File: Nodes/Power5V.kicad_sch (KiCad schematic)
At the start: 15 parts, among them U4 LT3970EMS#TRPBF

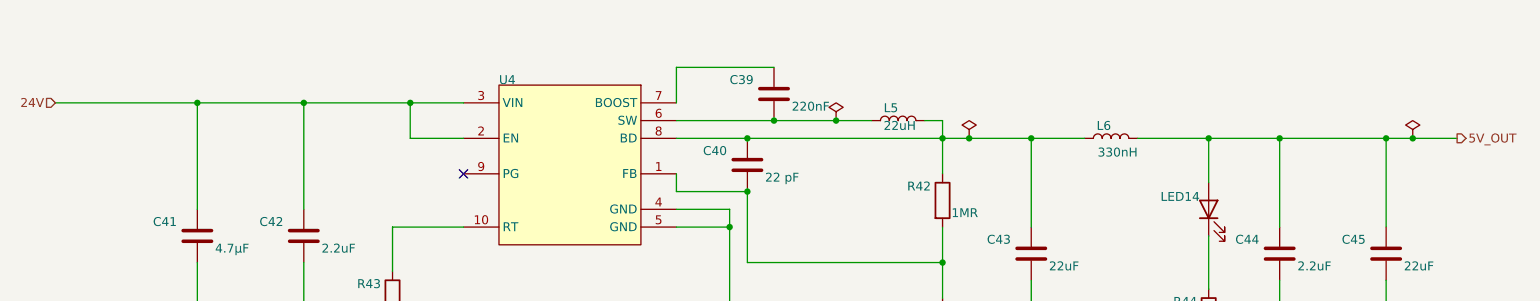
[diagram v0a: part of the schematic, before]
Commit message: Nodes v2.1.2 Improved
- Improved schematic design
- Added two 4.7 uF caps according to the datasheets of the microchips
- Other small changes
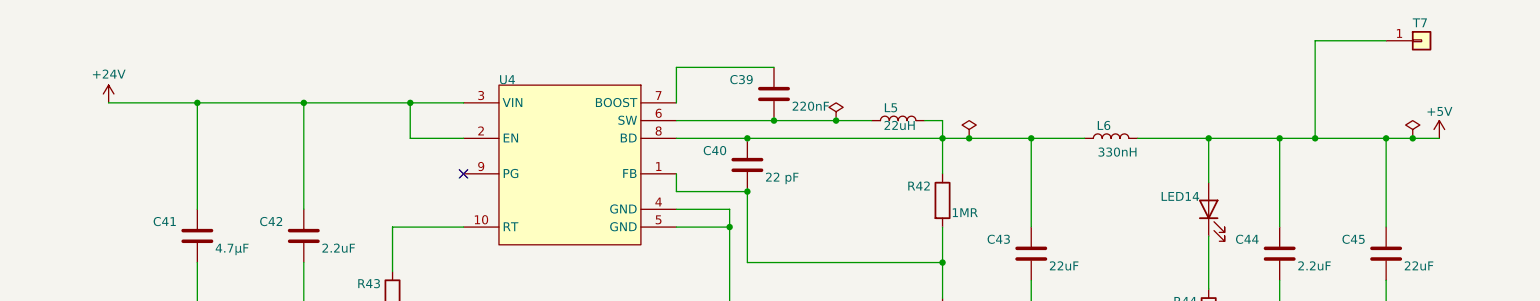
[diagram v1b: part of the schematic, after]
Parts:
- added T7: Conn_01x01, TestPoint:TestPoint_THTPad_D1.5mm_Drill0.7mm, symbol Connector_Generic:Conn_01x01
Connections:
- net 24V renamed +24V
- net 5V_OUT renamed +5V
- net +5V: now also T7.1 (Pin_1)

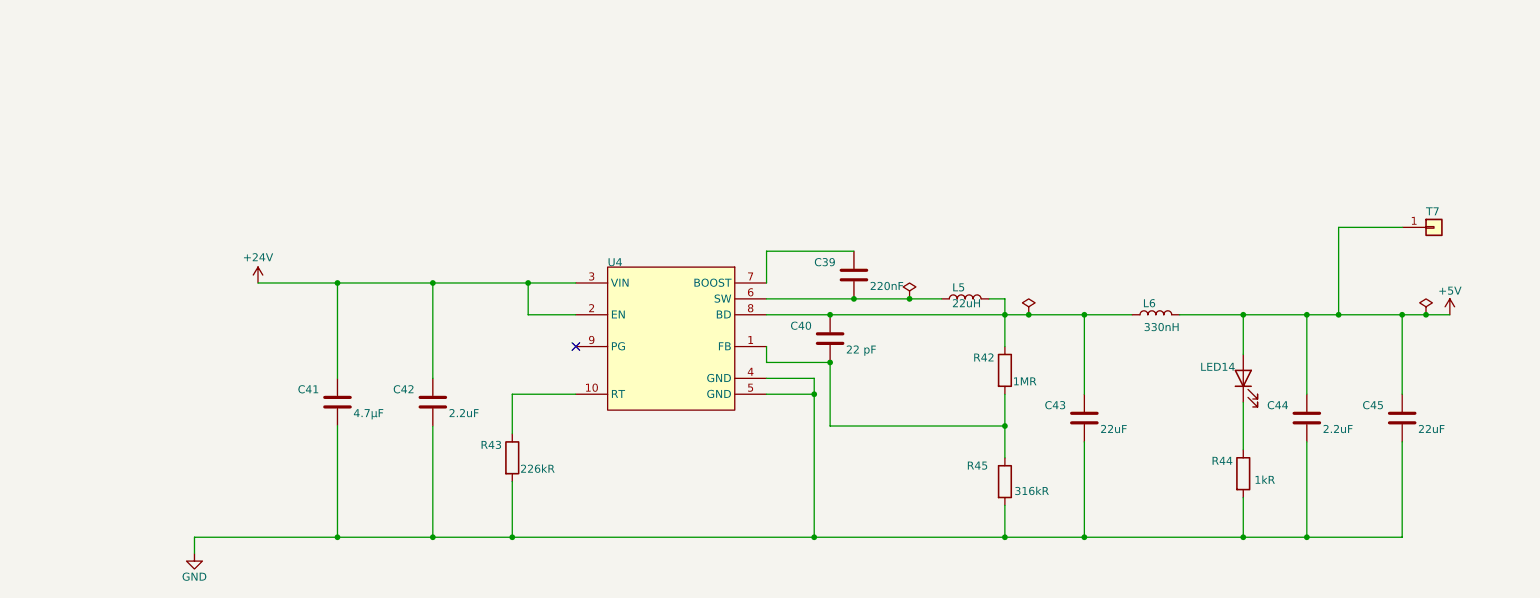
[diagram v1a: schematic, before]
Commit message: Nodes v2.2
- This version not compatible with BOB v.2.1.2 and older!
- Completely new layout design
- New power supply system with new voltage regulators
- New microchip STM32G431RBTx for the Analog Node
- New connection system (instead of 18 pin headers now 8 pin and pins were grouped by functions)
- Reduced size of the board by 5%
- Removed power switch for the Analog Node (because this functionality is now provided by a separate voltage regulator. for a more stable voltage)
- Removable ground from the holes added
- Layer numbers added
- Small improvements of the components information were made
- New oscillator for the Nodes
- Removed CAN1, so now only one CAN connection due to the capabilities of the new microchip
- Other small changes and fixes on the schematic and design
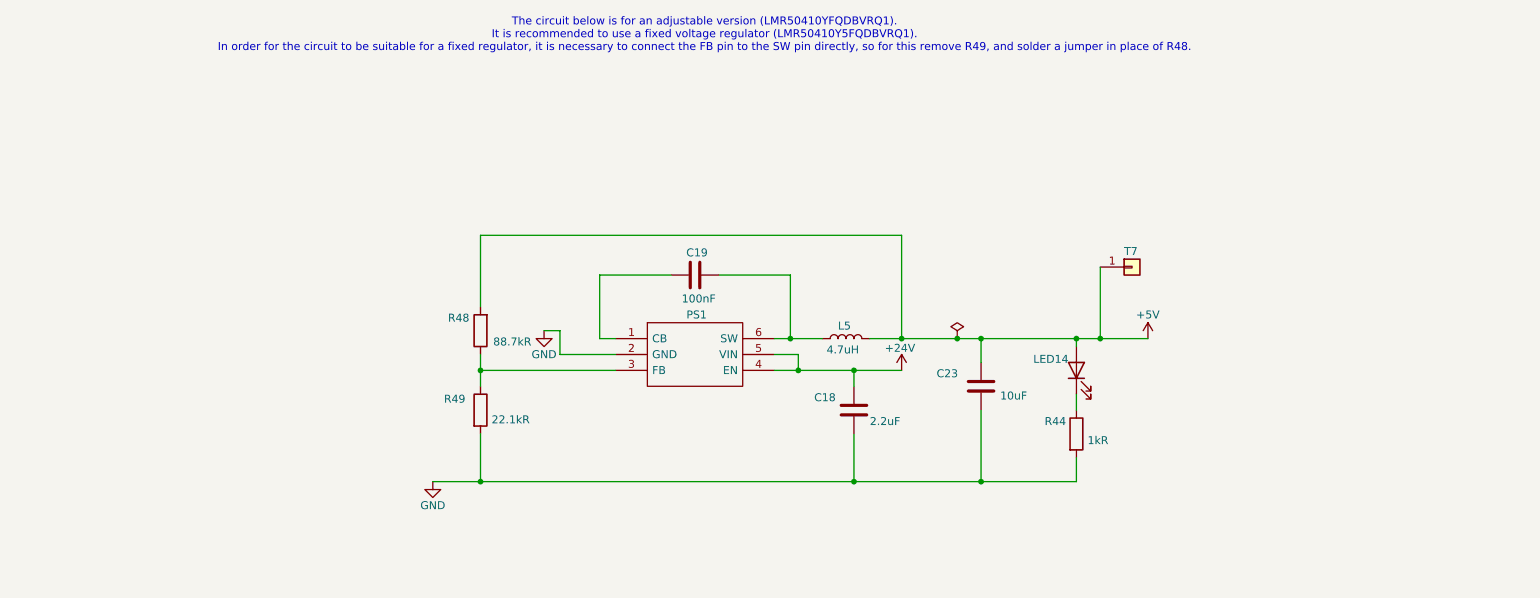
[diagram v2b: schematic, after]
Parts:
- removed C39: 220nF, Capacitor_SMD:C_0805_2012Metric_Pad1.18x1.45mm_HandSolder, symbol Device:C
- removed C40: 22 pF, Capacitor_SMD:C_0805_2012Metric_Pad1.18x1.45mm_HandSolder, symbol Device:C
- removed C41: 4.7µF, Capacitor_SMD:C_0805_2012Metric_Pad1.18x1.45mm_HandSolder, symbol Device:C
- removed C42, C44: 2.2uF, Capacitor_SMD:C_0805_2012Metric_Pad1.18x1.45mm_HandSolder, symbol Device:C
- removed C43, C45: 22 uF, Capacitor_SMD:C_0805_2012Metric_Pad1.18x1.45mm_HandSolder, symbol Device:C
- removed L6: 330nH, Inductor_SMD:L_0805_2012Metric_Pad1.15x1.40mm_HandSolder, symbol Device:L
- removed R42: 1MR, Resistor_SMD:R_0805_2012Metric_Pad1.20x1.40mm_HandSolder, symbol Device:R
- removed R43: 226kR, Resistor_SMD:R_0805_2012Metric_Pad1.20x1.40mm_HandSolder, symbol Device:R
- removed R45: 316kR, Resistor_SMD:R_0805_2012Metric_Pad1.20x1.40mm_HandSolder, symbol Device:R
- removed U4: LT3970EMS#TRPBF, Vault:LT-MS-10_N, symbol Untitled-altium-import:root_0_LT-LT3970_B-MS-10
- added C18: 2.2uF, Capacitor_SMD:C_0805_2012Metric_Pad1.18x1.45mm_HandSolder, symbol Device:C
- added C19: 100nF, Capacitor_SMD:C_0805_2012Metric_Pad1.18x1.45mm_HandSolder, symbol Device:C
- added C23: 10uF, Capacitor_SMD:C_0805_2012Metric_Pad1.18x1.45mm_HandSolder, symbol Device:C
- added PS1: LMR50410YFQDBVRQ1, Regulators:SOT95P280X145-6N, symbol Regulator_Switching:LMR50410YFQDBVRQ1
- added R48: 88.7kR, Resistor_SMD:R_0805_2012Metric_Pad1.20x1.40mm_HandSolder, symbol Device:R
- added R49: 22.1kR, Resistor_SMD:R_0805_2012Metric_Pad1.20x1.40mm_HandSolder, symbol Device:R
- L5: value 22uH -> 4.7uH; ALTIUM_VALUE 22uH -> (none); CHANNELS 1 -> (none); CORE MATERIAL Ferrite -> (none); DC RESISTANCE (DCR) 0.67R -> (none); INDUCTANCE-NOM (L) 22uH -> (none); INDUCTOR APPLICATION RF INDUCTOR -> (none); INDUCTOR TYPE GENERAL PURPOSE INDUCTOR -> (none); MAX CURRENT RATING 300mA -> (none); MAX OPERATING TEMPERATURE 125°C -> (none); MIN OPERATING TEMPERATURE -55°C -> (none); PINS 2 -> (none); REACH SVHC COMPLIANT Yes -> (none); ROHS COMPLIANT Yes -> (none); SELF RESONANT FREQUENCY 20MHz -> (none); SHAPE/SIZE DESCRIPTION RECTANGULAR PACKAGE -> (none); SHIELDING Shielded -> (none); SURFACE MOUNT Yes -> (none); TERMINAL PLACEMENT Dual Ended -> (none); TERMINATION One Surface -> (none); TEST FREQUENCY 2MHz -> (none); TOLERANCE 20% -> (none)
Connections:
- net +24V: now also C18.1, PS1.4 (EN), PS1.5 (VIN)
- net +5V: now also L5.2, C23.1, R48.2
- net GND: now also C18.2, C23.2, PS1.2 (GND), R49.2
- net at L5.1: now also C19.2, PS1.6 (SW)
- new net: C19.1, PS1.1 (CB)
- new net: PS1.3 (FB), R48.1, R49.1
- no-connect marks 1 -> 0
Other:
- note added: "The circuit below is for an adjustable version (LMR50410YFQDBVRQ1). It is recommended to use a fixed voltage regulator (LMR50410Y5FQDBVRQ1). In order for the circuit to be suitable for a fixed regulator, it is necessary to connect the FB pin to the SW pin directly, so for this remove R49, and solder a jumper in place of R48."
